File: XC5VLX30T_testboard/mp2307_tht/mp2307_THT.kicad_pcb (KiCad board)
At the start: 2 copper layers, 23.6 x 13.7 mm, 13 parts, among them J1 Inductor L, J2 Inductor_R, J4 Conn_01x06_Pin, U1 MP2307DN-LF-Z

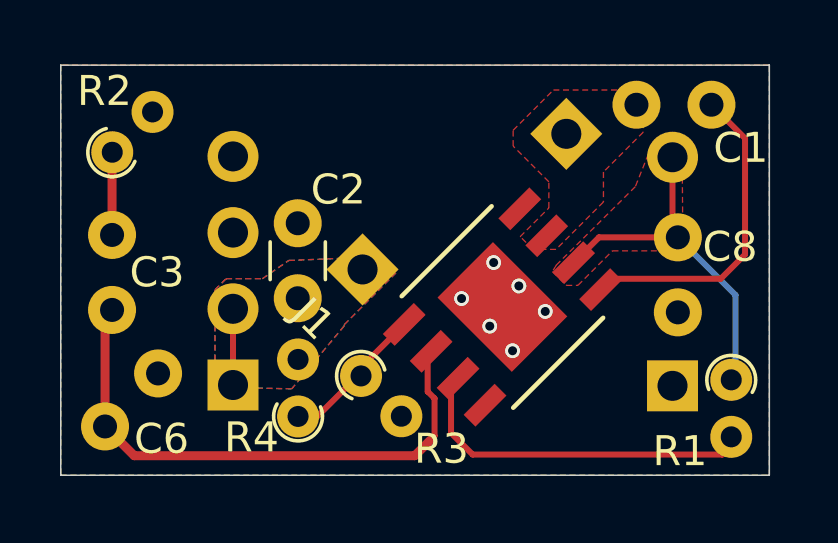
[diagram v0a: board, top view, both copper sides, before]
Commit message: update mp2307 tht resistor labels
resistor labels on mp2307 tht board now match datasheet
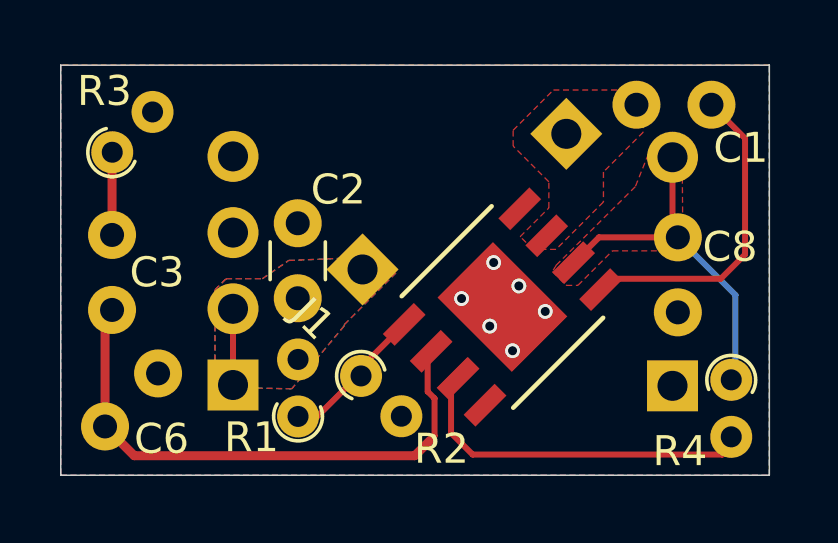
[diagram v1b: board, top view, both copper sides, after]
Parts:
- renumbered R4 to R1, R3 to R2, R2 to R3, R1 to R4
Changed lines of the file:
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@@
 		(descr "Resistor, Axial_DIN0204 series, Axial, Vertical, pin pitch=1.9mm, 0.167W, length*diameter=3.6*1.6mm^2, http://cdn-reichelt.de/documents/datenblatt/B400/1_4W%23YAG.pdf")
 		(tags "Resistor Axial_DIN0204 series Axial Vertical pin pitch 1.9mm 0.167W length 3.6mm diameter 1.6mm")
-		(property "Reference" "R2"
+		(property "Reference" "R3"
 			(at 1.258554 -1.626346 180)
 			(layer "F.SilkS")
@@
 		(descr "Resistor, Axial_DIN0204 series, Axial, Vertical, pin pitch=1.9mm, 0.167W, length*diameter=3.6*1.6mm^2, http://cdn-reichelt.de/documents/datenblatt/B400/1_4W%23YAG.pdf")
 		(tags "Resistor Axial_DIN0204 series Axial Vertical pin pitch 1.9mm 0.167W length 3.6mm diameter 1.6mm")
-		(property "Reference" "R1"
-			(at 2.38 1.71 180)
+		(property "Reference" "R4"
+			(at 2.38 1.71 0)
 			(layer "F.SilkS")
 			(effects
@@
 		(descr "Resistor, Axial_DIN0204 series, Axial, Vertical, pin pitch=1.9mm, 0.167W, length*diameter=3.6*1.6mm^2, http://cdn-reichelt.de/documents/datenblatt/B400/1_4W%23YAG.pdf")
 		(tags "Resistor Axial_DIN0204 series Axial Vertical pin pitch 1.9mm 0.167W length 3.6mm diameter 1.6mm")
-		(property "Reference" "R4"
+		(property "Reference" "R1"
 			(at -0.7 -1.55 0)
 			(layer "F.SilkS")
@@
 		(fp_arc
 			(start 0.3048 -2.5019)
-			(mid 0 -2.197091)
+			(mid 0 -2.19709)
 			(end -0.3048 -2.5019)
 			(stroke
@@
 		(descr "Resistor, Axial_DIN0204 series, Axial, Vertical, pin pitch=1.9mm, 0.167W, length*diameter=3.6*1.6mm^2, http://cdn-reichelt.de/documents/datenblatt/B400/1_4W%23YAG.pdf")
 		(tags "Resistor Axial_DIN0204 series Axial Vertical pin pitch 1.9mm 0.167W length 3.6mm diameter 1.6mm")
-		(property "Reference" "R3"
-			(at 3.613316 -0.176777 180)
+		(property "Reference" "R2"
+			(at 3.613316 -0.176777 360)
 			(layer "F.SilkS")
 			(effects
